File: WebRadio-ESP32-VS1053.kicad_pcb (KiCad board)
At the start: 2 copper layers, 91.5 x 61 mm, 77 parts, among them J1 Conn_01x02, J2 JST PH 2mm, J3 JST PH 2mm, J4 AudioJack3, J6 JST PH 2mm, J7 JST PH 2mm, J8 Conn_01x05, J9 Conn_01x04, P1 USB_C_Plug_USB2.0, SW1 SW_Push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

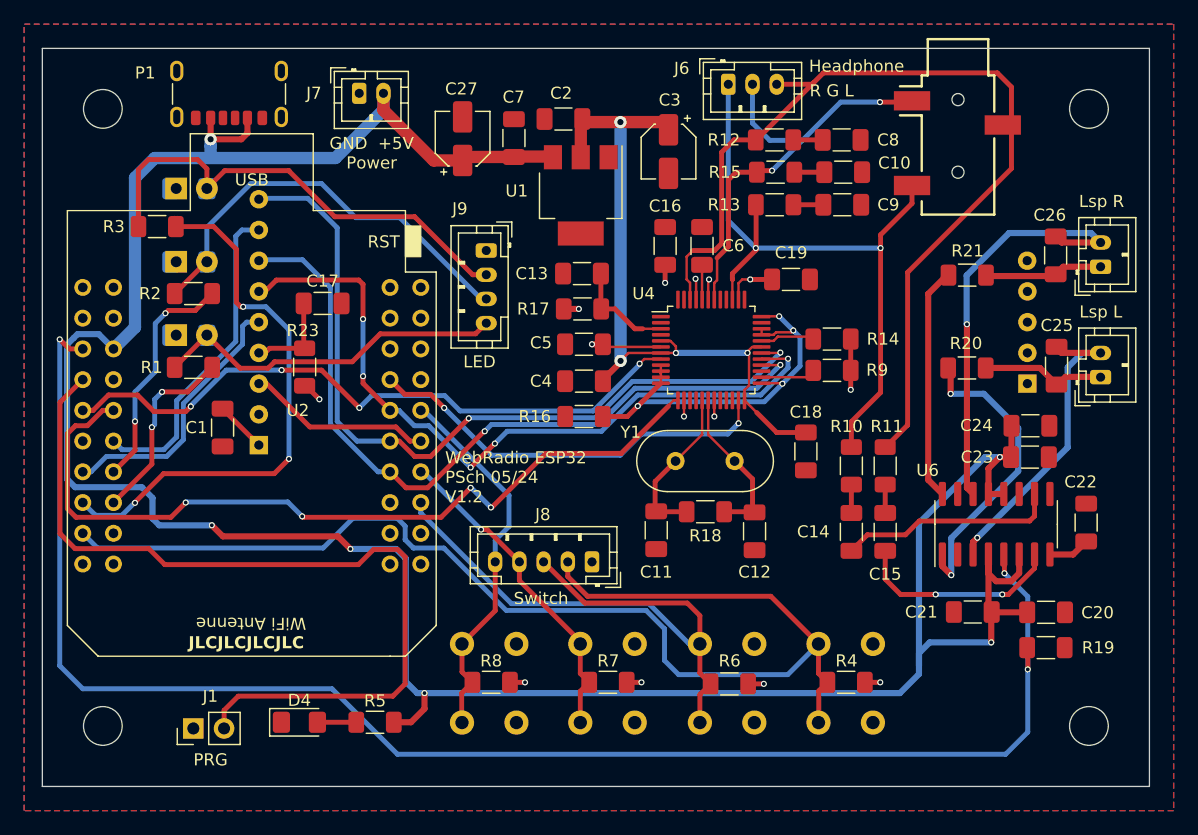
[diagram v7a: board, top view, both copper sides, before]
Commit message: change some silkscreen data
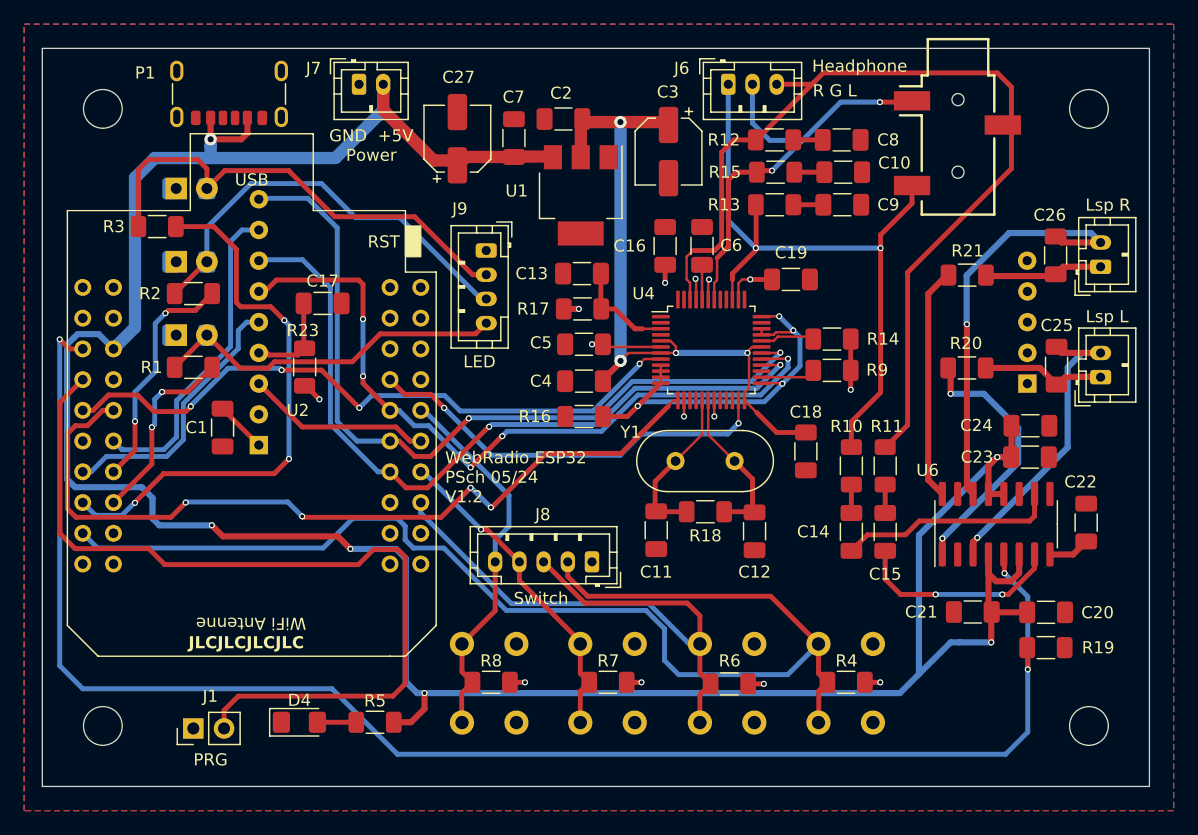
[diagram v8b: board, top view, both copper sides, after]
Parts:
- C27, C3: footprint Capacitor_SMD:CP_Elec_4x5.4 -> Capacitor_SMD:CP_Elec_5x5.4
- DS2: footprint psch:TFT2.2_SPI_5P_SD -> lib_psch:TFT2.2_SPI_5P_SD
- moved J7 0.75 mm to (139.7, 63.0)
- moved C27 0.43 mm to (147.8, 67.5)
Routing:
- net Net-(U6-LOUT+): track 25.3 -> 21.9 mm
- net DISP_CS: track 14.8 -> 15.4 mm
- net +5V: track 224.3 -> 224.9 mm
